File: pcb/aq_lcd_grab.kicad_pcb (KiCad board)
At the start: 4 copper layers, 32 x 50 mm, 12 parts, among them J1 Conn_01x39_Socket, J2 Conn_01x39_Socket, J3 Conn_01x03_Socket, J5 Conn_01x03_Pin, U1 STM32F030C8Tx, U2 Conn_01x14

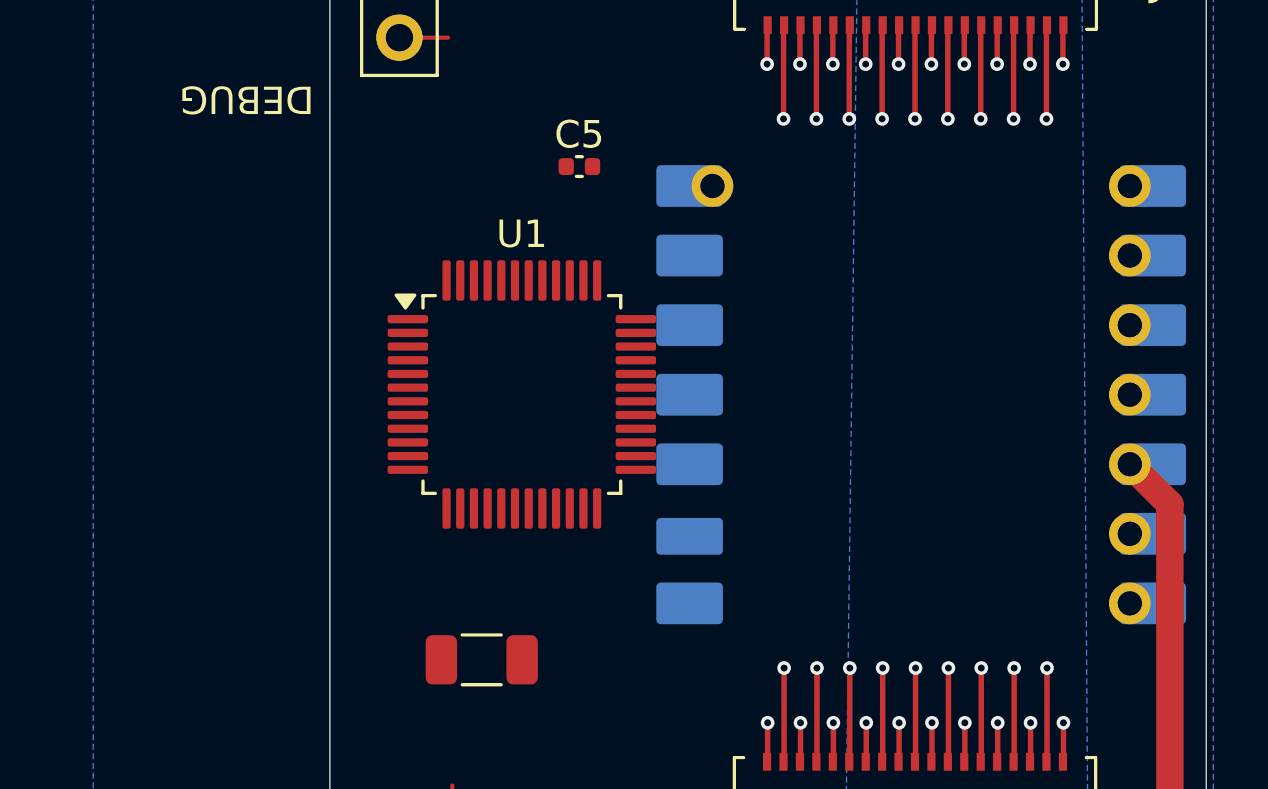
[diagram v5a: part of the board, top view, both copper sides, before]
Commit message: Straighten flex pass-through traces; add script that did the work
Replaces each flex net's inner-layer routing (a length-tuning serpentine
in many cases) with a single straight segment between the two F.Cu<->B.Cu
vias. F.Cu fanout stubs and vias are untouched. 452 inner segments out,
39 in.

Co-Authored-By: Claude Opus 4.7 (1M context) <noreply@anthropic.com>
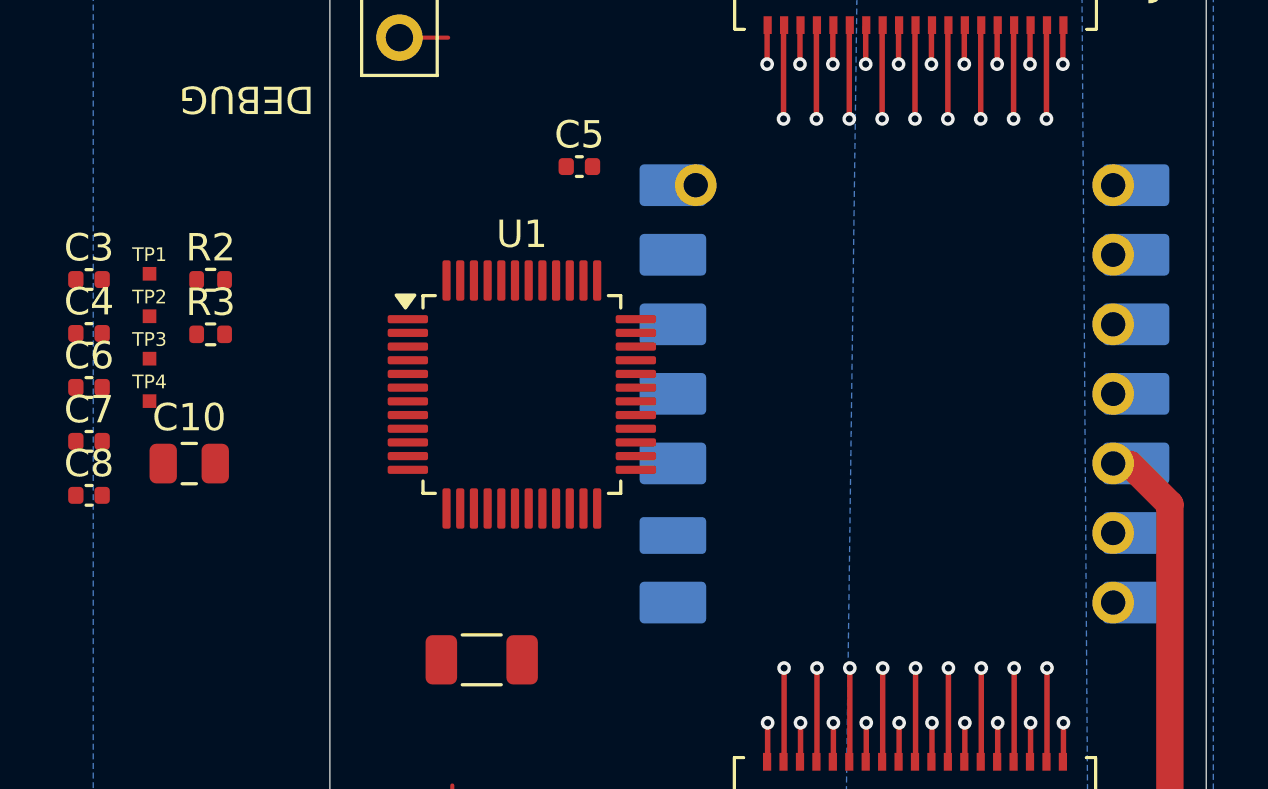
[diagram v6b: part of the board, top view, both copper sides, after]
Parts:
- added C10: 22u, Capacitor_SMD:C_0805_2012Metric, F.Cu at (45.7, 53.5)
- added C3: 100n, Capacitor_SMD:C_0402_1005Metric, F.Cu at (42.0, 46.8)
- added C4: 100n, Capacitor_SMD:C_0402_1005Metric, F.Cu at (42.0, 48.8)
- added C6: 1u, Capacitor_SMD:C_0402_1005Metric, F.Cu at (42.0, 50.7)
- added C7: 4.7u, Capacitor_SMD:C_0402_1005Metric, F.Cu at (42.0, 52.7)
- added C8: 100n, Capacitor_SMD:C_0402_1005Metric, F.Cu at (42.0, 54.7)
- added R2: 10k, Resistor_SMD:R_0402_1005Metric, F.Cu at (46.4, 46.8)
- added R3: 1k, Resistor_SMD:R_0402_1005Metric, F.Cu at (46.4, 48.8)
- added TP1: TestPoint, test_points:TestPoint_Pad_0.5x0.5mm, F.Cu at (44.2, 46.6)
- added TP2: TestPoint, test_points:TestPoint_Pad_0.5x0.5mm, F.Cu at (44.2, 48.1)
- added TP3: TestPoint, test_points:TestPoint_Pad_0.5x0.5mm, F.Cu at (44.2, 49.7)
- added TP4: TestPoint, test_points:TestPoint_Pad_0.5x0.5mm, F.Cu at (44.2, 51.2)
- C5: value 4.7u -> 100n
- U1: value STM32F030C8Tx -> STM32F103C8Tx
- moved U2 0.61 mm to (71.8, 51.0)
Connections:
- U1 pad 20: LED_STATUS -> BOOT1
- U1 pad 35: (no net) -> GND
- U1 pad 36: (no net) -> +3V3
- U1 pad 41: PB5 -> LED_STATUS
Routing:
- net GND_1: track 36.9 -> 35.5 mm
- net DB3: track 36.8 -> 35.5 mm
- net DB1: track 36.8 -> 35.5 mm
- net VCC_33: track 36.6 -> 35.5 mm
- net P34: track 27.9 -> 26.9 mm
- net VCC_35: track 36.5 -> 35.5 mm
- net DC: track 36.4 -> 35.5 mm
- net P25: track 36.4 -> 35.5 mm
- net P21: track 36.4 -> 35.5 mm
- net DB7: track 36.2 -> 35.5 mm
- net P29: track 36.2 -> 35.5 mm
- net VCC_37: track 36.2 -> 35.5 mm
- net DB15: track 36.2 -> 35.5 mm
- net DB11: track 36.2 -> 35.5 mm
- net P39: track 36.1 -> 35.5 mm
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
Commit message: Straightener: 45° jog plan based on top-via y-band
J2 side now matches the hand-routed pattern: nets in the y=33.24 band
dodge LEFT then RIGHT, y=36.04 nets dodge RIGHT then LEFT, even-pin
nets (shallow bands, In1.Cu) go straight through. J1 side still uses
J2 offsets verbatim — works for the shallow bands but the deep-band
distances are wrong (J1 obstacles sit closer to the via), leaving DRC
violations on adjacent same-layer pairs to clean up next.

Co-Authored-By: Claude Opus 4.7 (1M context) <noreply@anthropic.com>
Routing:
- net P29: track 35.5 -> 36.1 mm
- net DB7: track 35.5 -> 36.1 mm
- net VCC_37: track 35.5 -> 36.1 mm
- net VCC_33: track 35.5 -> 36.1 mm
- net P25: track 35.5 -> 36.1 mm
- net P21: track 35.5 -> 36.1 mm
- net GND_1: track 35.5 -> 36.1 mm
- net DB3: track 35.5 -> 36.1 mm
- net DB15: track 35.5 -> 36.1 mm
- net DB11: track 35.5 -> 36.1 mm
- net P39: track 35.5 -> 36.1 mm
- net GND_19: track 35.5 -> 36.1 mm
- net VCC_35: track 35.5 -> 36.1 mm
- net P31: track 35.5 -> 36.1 mm
- net P27: track 35.5 -> 36.1 mm
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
